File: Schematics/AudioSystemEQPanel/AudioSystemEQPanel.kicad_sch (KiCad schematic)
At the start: 47 parts, among them J1 AudioJack3, J2 AudioJack3, U1 OPA2134, U2 OPA2134, U3 OPA2134, U4 OPA2134

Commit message: added code debug function namespace, fixed eq-panel resistor values
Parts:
- removed R22, R23: 1k, symbol Device:R
- added RV4: 10k, symbol Device:R_Potentiometer_Dual
- R10, R9: value 62k -> 68k
- R13, R14: value 2.4k -> 2.6k
- R16, R19: value 1k -> 510
- R17, R20: value 1k -> 750
- R2, R3: value 750 -> 2k
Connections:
- net GND: now also RV4.2, RV4.5
- net at R21.1, U4.2 (-): now also RV4.6
- net at R24.1, U4.6 (-): now also RV4.3

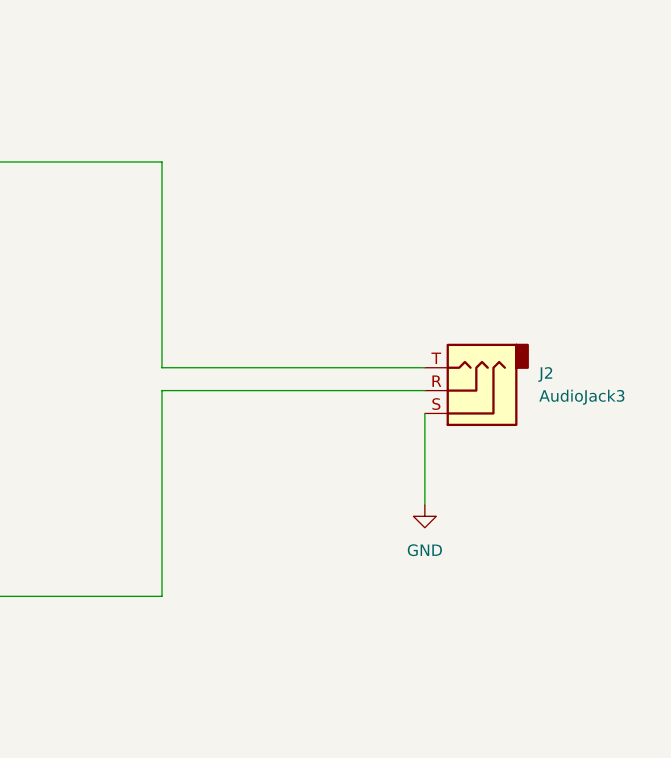
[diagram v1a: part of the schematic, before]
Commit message: added full audio system schematic (not completed)
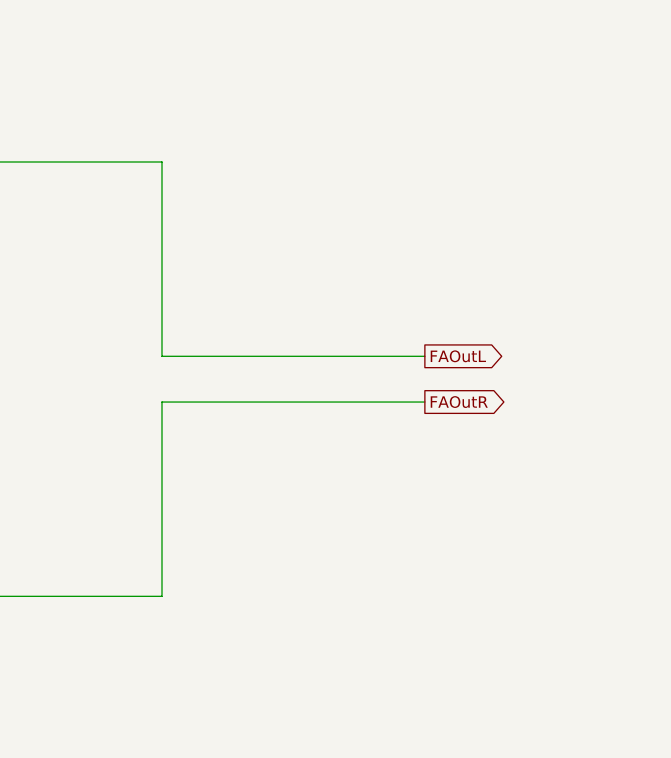
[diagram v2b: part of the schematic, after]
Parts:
- removed J2: AudioJack3, symbol Connector_Audio:AudioJack3
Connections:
- net FAOutL: now reaches R21.2, U4.1
- net FAOutR: now reaches R24.2, U4.7
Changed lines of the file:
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@@
 	(wire
 		(pts
-			(xy 320.04 123.19) (xy 349.25 123.19)
+			(xy 320.04 121.92) (xy 349.25 121.92)
 		)
 		(stroke
@@
 	(wire
 		(pts
-			(xy 320.04 100.33) (xy 320.04 123.19)
+			(xy 320.04 100.33) (xy 320.04 121.92)
 		)
 		(stroke
@@
 	(wire
 		(pts
-			(xy 320.04 125.73) (xy 349.25 125.73)
+			(xy 320.04 127) (xy 349.25 127)
 		)
 		(stroke
@@
 	(wire
 		(pts
-			(xy 320.04 148.59) (xy 320.04 125.73)
+			(xy 320.04 148.59) (xy 320.04 127)
 		)
 		(stroke
@@
 	(wire
 		(pts
-			(xy 349.25 128.27) (xy 349.25 138.43)
-		)
-		(stroke
-			(width 0)
-			(type default)
-		)
-	)
-	(wire
-		(pts
 			(xy 92.71 171.45) (xy 92.71 180.34)
 		)
@@
 		)
 	)
+	(global_label "FAOutR"
+		(shape output)
+		(at 349.25 127 0)
+		(fields_autoplaced yes)
+		(effects
+			(font
+				(size 1.27 1.27)
+			)
+			(justify left)
+		)
+		(property "Intersheetrefs" "${INTERSHEET_REFS}"
+			(at 358.8876 127 0)
+			(effects
+				(font
+					(size 1.27 1.27)
+				)
+				(justify left)
+				(hide yes)
+			)
+		)
+	)
 	(global_label "R_HIGH"
 		(shape input)
@@
 		)
 	)
+	(global_label "FAOutL"
+		(shape output)
+		(at 349.25 121.92 0)
+		(fields_autoplaced yes)
+		(effects
+			(font
+				(size 1.27 1.27)
+			)
+			(justify left)
+		)
+		(property "Intersheetrefs" "${INTERSHEET_REFS}"
+			(at 358.6457 121.92 0)
+			(effects
+				(font
+					(size 1.27 1.27)
+				)
+				(justify left)
+				(hide yes)
+			)
+		)
+	)
 	(global_label "L_MID"
 		(shape output)
@@
 	)
 	(symbol
-		(lib_id "power:GND")
-		(at 349.25 138.43 0)
-		(unit 1)
-		(exclude_from_sim no)
-		(in_bom yes)
-		(on_board yes)
-		(dnp no)
-		(fields_autoplaced yes)
-		(property "Reference" "#PWR018"
-			(at 349.25 144.78 0)
-			(effects
-				(font
-					(size 1.27 1.27)
-				)
-				(hide yes)
-			)
-		)
-		(property "Value" "GND"
-			(at 349.25 143.51 0)
-			(effects
-				(font
-					(size 1.27 1.27)
-				)
-			)
-		)
-		(property "Footprint" ""
-			(at 349.25 138.43 0)
-			(effects
-				(font
-					(size 1.27 1.27)
-				)
-				(hide yes)
-			)
-		)
-		(property "Datasheet" ""
-			(at 349.25 138.43 0)
-			(effects
-				(font
-					(size 1.27 1.27)
-				)
-				(hide yes)
-			)
-		)
-		(property "Description" "Power symbol creates a global label with name \"GND\" , ground"
-			(at 349.25 138.43 0)
-			(effects
-				(font
-					(size 1.27 1.27)
-				)
-				(hide yes)
-			)
-		)
-		(pin "1"
-		)
-		(instances
-			(project "AudioSystemEQPanel"
-				(path "/d171f5e5-58fa-445c-b596-876d1e770727"
-					(reference "#PWR018")
-					(unit 1)
-				)
-			)
-		)
-	)
-	(symbol
 		(lib_id "Device:R")
 		(at 180.34 167.64 180)
@@
 					(unit 1)
 				)
-			)
-		)
-	)
-	(symbol
-		(lib_id "Connector_Audio:AudioJack3")
-		(at 354.33 125.73 180)
-		(unit 1)
-		(exclude_from_sim no)
-		(in_bom yes)
-		(on_board yes)
-		(dnp no)
-		(fields_autoplaced yes)
-		(property "Reference" "J2"
-			(at 361.95 123.8249 0)
-			(effects
-				(font
-					(size 1.27 1.27)
-				)
-				(justify right)
-			)
-		)
-		(property "Value" "AudioJack3"
-			(at 361.95 126.3649 0)
-			(effects
-				(font
-					(size 1.27 1.27)
-				)
-				(justify right)
-			)
-		)
-		(property "Footprint" ""
-			(at 354.33 125.73 0)
-			(effects
-				(font
-					(size 1.27 1.27)
-				)
-				(hide yes)
-			)
-		)
-		(property "Datasheet" "~"
-			(at 354.33 125.73 0)
-			(effects
-				(font
-					(size 1.27 1.27)
-				)
-				(hide yes)
-			)
-		)
-		(property "Description" "Audio Jack, 3 Poles (Stereo / TRS)"
-			(at 354.33 125.73 0)
-			(effects
-				(font
-					(size 1.27 1.27)
-				)
-				(hide yes)
-			)
-		)
-		(pin "T"
-		)
-		(pin "R"
-		)
-		(pin "S"
-		)
-		(instances
-			(project ""
-				(path "/d171f5e5-58fa-445c-b596-876d1e770727"
-					(reference "J2")
-					(unit 1)
-				)
